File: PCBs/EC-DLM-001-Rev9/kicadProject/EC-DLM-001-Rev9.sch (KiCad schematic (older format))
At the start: 70 parts, among them J1 DMX out, J10 RJ45, J11 RJ45, J12 BARREL_JACK, J14 3.3V, J15 DMX Test pins, J2 DMX in, J20 CONN_01X04, J22 btn 6, J23 btn 3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

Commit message: Working on DLM pcb rev9
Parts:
- removed C23, C24: 100n, Capacitors_SMD:C_0603_HandSoldering, symbol C
- removed C7: 100u, Capacitors_SMD:C_0603_HandSoldering, symbol CP1
- removed J22: btn 6, Pin_Headers:Pin_Header_Straight_1x01_Pitch2.54mm, symbol CONN_01X01
- removed J23: btn 3, Pin_Headers:Pin_Header_Straight_1x01_Pitch2.54mm, symbol CONN_01X01
- removed J?: CONN_01X14, symbol CONN_01X14
- removed R15, R16: 10k, Resistors_SMD:R_0603_HandSoldering, symbol R
- removed R22, R23: 220, Resistors_SMD:R_0603_HandSoldering, symbol R
- added L1: Fer Bead, Inductors_SMD:L_0603_HandSoldering, symbol Ferrite_Bead
- added L4: 10uH, Inductors_SMD:L_0603_HandSoldering, symbol L
- F1: renamed from F?; footprint (none) -> Fuse_Holders_and_Fuses:Fuseholder5x20_horiz_open_lateral_Type-II
- J20: value CONN_01X04 -> BTN-VDD; symbol CONN_01X04 -> CONN_01X02
- gave numbers to parts that had none: 1
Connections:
- net labels added: AVCC
- net labels removed: PE3, PE4, PE5
- wire segments 304 -> 290
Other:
- moved on the sheet: C1, C17, C2, C21, C22, C3, C5, C6, C8, D3, D4, F1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

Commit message: TR04 + DLM01 REV9 adjustments.
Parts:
- removed JP1: Jumper_NC_Small, symbol Jumper_NC_Small
- added C4: 1000u, Capacitors_THT:CP_Radial_D14.0mm_P7.50mm, symbol CP1
- added J13: Bluetooth Module, Pin_Headers:Pin_Header_Straight_1x06_Pitch2.54mm, symbol CONN_01X06
- added L5: 10uH, Diodes_THT:D_DO-15_P12.70mm_Horizontal, symbol L
- L1, L4: footprint Inductors_SMD:L_0603_HandSoldering -> Diodes_THT:D_DO-15_P12.70mm_Horizontal
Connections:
- net +5V: now also J13.2 (P2)
- net AVCC: now also C4.1
- net AnalogGND: now also C4.2, L5.2
- net GND: now also J2.1, J13.3 (P3), L5.1
- net BT_TX: now reaches U3.22 (MISO/RXD1/~OC0DLS~/PC6)
- net BT_TX: now also J13.4 (P4)
- net BTN3: no longer names the net of U3.33 (PD7/TXD1/D+/SCK/CLKOUT/EVOUT)
- net BTN4: no longer names the net of U3.26 (OC0A/PD0)
- net L7_OUT_3.3: no longer names the net of U3.4 (AC1OUT/AC6/ADC6/PA6)
- net L8_OUT_3.3: no longer names the net of U3.5 (AC0OUT/AC7/ADC7/PA7)
- net STrig1: no longer names the net of U3.16 (SDAIN/SDA/~OC0ALS~/OC0A/PC0)
- net STrig2: no longer names the net of U3.17 (SCLIN/SCL/XCK0/OC0AHS/OC0B/PC1)
- net STrig3: no longer names the net of U3.18 (SDAOUT/RXD0/~OC0BLS~/OC0C/PC2)
- net STrig4: no longer names the net of U3.19 (SCLOUT/TXD0/OC0BHS/OC0D/PC3)
- net STrig5: no longer names the net of U3.20 (~SS~/~OC0CLS~/OC1A/PC4)
- net STrig6 renamed BT_RX
- net BT_RX: now also J13.5 (P5)
- no-connect marks 35 -> 45
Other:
- note added: "2 Buttons circuit"
- note added: "Bluetooth Interface (SPI)"
- note added: "DMX interface (UART)"
- note added: "External boards interfaces"
- note added: "LCD interface (SPI)"
- note added: "LED Signal 3.3v to 5V step up"
- note added: "PDI debug/prog interface"
- note added: "Power supply for microcontroller and analog"
- note added: "Rotary encoder circuit"
- note added: "User feedback LEDs"
- note added: "XMega power filtering"
- moved on the sheet: F1, L1, L4

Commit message: New Main board.
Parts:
- removed J14: 3.3V, Pin_Headers:Pin_Header_Straight_1x02_Pitch2.54mm, symbol CONN_01X02
- removed L1: Fer Bead, Diodes_THT:D_DO-15_P12.70mm_Horizontal, symbol Ferrite_Bead
- added C19: 100n, Capacitors_SMD:C_0805_HandSoldering, symbol CP1
- added C20: 68u, Capacitors_SMD:C_0805_HandSoldering, symbol CP1
- added C7: 39p, Capacitors_SMD:C_0805_HandSoldering, symbol CP1
- added D2: D_Schottky, Diodes_THT:D_A-405_P5.08mm_Vertical_AnodeUp, symbol D_Schottky
- added R11: 200k, Resistors_SMD:R_0805_HandSoldering, symbol R
- added R12: 500, Resistors_SMD:R_0805_HandSoldering, symbol R
- added R5: 17.3k, Resistors_SMD:R_0805_HandSoldering, symbol R
- added R8: 150k, Resistors_SMD:R_0805_HandSoldering, symbol R
- added U6: LM2621, Housings_SSOP:VSSOP-8_3.0x3.0mm_Pitch0.65mm, symbol LM2621
- C10, C11, C12, C13, C14, C18, C21, C22, C3, C6, C8, C9: footprint Capacitors_SMD:C_0603_HandSoldering -> Capacitors_SMD:C_0805_HandSoldering
- C17: footprint Capacitors_THT:CP_Radial_D14.0mm_P7.50mm -> Capacitors_THT:CP_Radial_D13.0mm_P5.00mm
- C4: value 1000u -> 22u; footprint Capacitors_THT:CP_Radial_D14.0mm_P7.50mm -> Capacitors_SMD:C_0805_HandSoldering
- L2, L3: footprint Inductors_SMD:L_0603_HandSoldering -> Inductors_SMD:L_0805_HandSoldering
- L4: value 10uH -> 6.8uH; footprint Diodes_THT:D_DO-15_P12.70mm_Horizontal -> Inductors_SMD:L_0805_HandSoldering
- L5: footprint Diodes_THT:D_DO-15_P12.70mm_Horizontal -> Inductors_SMD:L_0805_HandSoldering
- R1, R10, R17, R18, R24, R25, R4, R7, R9: footprint Resistors_SMD:R_0603_HandSoldering -> Resistors_SMD:R_0805_HandSoldering
- U1: footprint TO_SOT_Packages_THT:TO-220_Vertical -> TO_SOT_Packages_THT:TO-220-3_Vertical
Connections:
- net labels added: 12v
- wire segments 291 -> 387
- no-connect marks 45 -> 43
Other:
- note added: "PDI debug/prog"
- note added: "Power supply for microcontroller (up) and analog (down)"
- note removed: "PDI debug/prog interface"
- note removed: "Power supply for microcontroller and analog"
- moved on the sheet: C1, C17, C2, C5, F1, J12, J3, J5, L4, L5, R2, R3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

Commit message: Revision board rev9
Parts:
- removed C20: 68u, Capacitors_SMD:C_0805_HandSoldering, symbol CP1
- removed R12: 500, Resistors_SMD:R_0805_HandSoldering, symbol R
- removed U6: LM2621, Housings_SSOP:VSSOP-8_3.0x3.0mm_Pitch0.65mm, symbol LM2621
- added C20, C23, C24, C25, C26, C27, C28, C29, C30: 100n, symbol C
- added U6: LM2577, TO_SOT_Packages_THT:TO-220-5_Vertical, symbol LM2577
- C16, C2: value 10u -> 10u-tant
- C19: value 100n -> 680u; footprint Capacitors_SMD:C_0805_HandSoldering -> Capacitors_THT:CP_Radial_D13.0mm_P7.50mm
- C4: value 22u -> 0.33u; footprint Capacitors_SMD:C_0805_HandSoldering -> Capacitors_THT:CP_Radial_D5.0mm_P2.50mm
- C7: value 39p -> 0.1u; footprint Capacitors_SMD:C_0805_HandSoldering -> Capacitors_THT:CP_Radial_D5.0mm_P2.50mm
- D2: value D_Schottky -> 1N5821; footprint Diodes_THT:D_A-405_P5.08mm_Vertical_AnodeUp -> TO_SOT_Packages_THT:TO-220-2_Vertical
- L4: value 6.8uH -> 100uH; footprint Inductors_SMD:L_0805_HandSoldering -> Inductors_THT:L_Radial_D9.5mm_P5.00mm_Fastron_07HVP
- L5: footprint Inductors_SMD:L_0805_HandSoldering -> Inductors_THT:L_Axial_L9.5mm_D4.0mm_P5.08mm_Vertical_Fastron_SMCC
- R11: value 200k -> 2k; footprint Resistors_SMD:R_0805_HandSoldering -> Resistors_THT:R_Axial_DIN0207_L6.3mm_D2.5mm_P10.16mm_Horizontal
- R5: footprint Resistors_SMD:R_0805_HandSoldering -> Resistors_THT:R_Axial_DIN0207_L6.3mm_D2.5mm_P10.16mm_Horizontal
- R8: value 150k -> 2.2k; footprint Resistors_SMD:R_0805_HandSoldering -> Resistors_THT:R_Axial_DIN0207_L6.3mm_D2.5mm_P10.16mm_Horizontal
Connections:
- net labels added: 3.3v
- wire segments 387 -> 304
- no-connect marks 43 -> 33
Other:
- note added: "Bluetooth (SPI)"
- note removed: "Bluetooth Interface (SPI)"
- moved on the sheet: C19, C4, C7, D2, D3, L4, R11, R5, R8

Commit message: New board pour production
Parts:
- C20, C23, C24, C25, C26, C27, C28, C29, C30: footprint (none) -> Capacitors_THT:CP_Radial_D6.3mm_P2.50mm

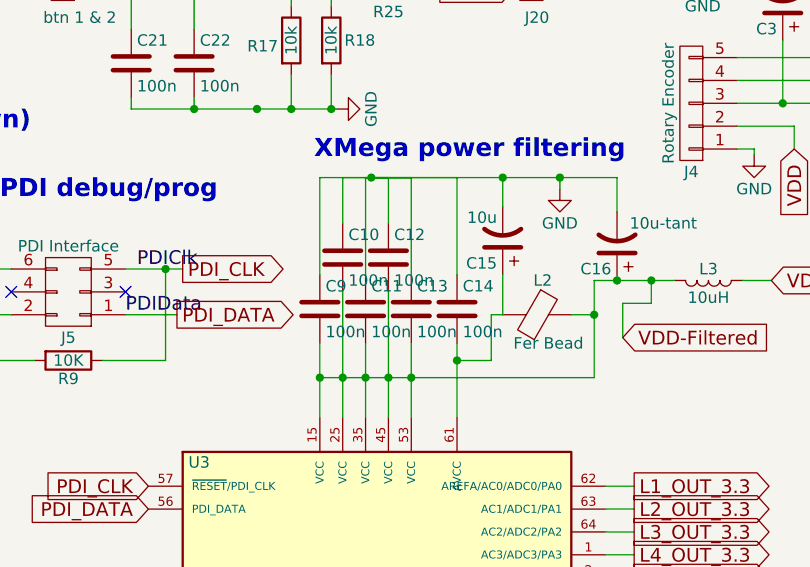
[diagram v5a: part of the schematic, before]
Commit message: Fixed screen corruption problem.
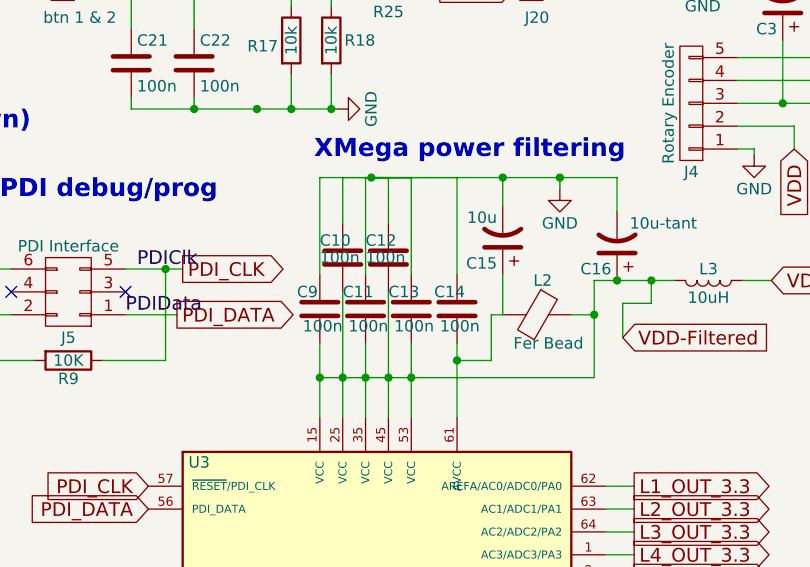
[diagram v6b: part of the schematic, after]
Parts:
- D2: footprint TO_SOT_Packages_THT:TO-220-2_Vertical -> Diodes_THT:D_DO-201AD_P15.24mm_Horizontal
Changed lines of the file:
@@
 U 1 1 59A1EB98
 P 5250 2400
-F 0 "C9" H 5275 2500 50  0000 L CNN
-F 1 "100n" H 5275 2300 50  0000 L CNN
+F 0 "C9" H 5150 2475 50  0000 L CNN
+F 1 "100n" H 5175 2325 50  0000 L CNN
 F 2 "Capacitors_SMD:C_0805_HandSoldering" H 5288 2250 50  0001 C CNN
 F 3 "" H 5250 2400 50  0001 C CNN
@@
 U 1 1 59A1EBF3
 P 5350 2175
-F 0 "C10" H 5375 2275 50  0000 L CNN
-F 1 "100n" H 5375 2075 50  0000 L CNN
+F 0 "C10" H 5250 2250 50  0000 L CNN
+F 1 "100n" H 5250 2175 50  0000 L CNN
 F 2 "Capacitors_SMD:C_0805_HandSoldering" H 5388 2025 50  0001 C CNN
 F 3 "" H 5350 2175 50  0001 C CNN
@@
 U 1 1 59A1EC2A
 P 5450 2400
-F 0 "C11" H 5475 2500 50  0000 L CNN
-F 1 "100n" H 5475 2300 50  0000 L CNN
+F 0 "C11" H 5350 2475 50  0000 L CNN
+F 1 "100n" H 5375 2325 50  0000 L CNN
 F 2 "Capacitors_SMD:C_0805_HandSoldering" H 5488 2250 50  0001 C CNN
 F 3 "" H 5450 2400 50  0001 C CNN
@@
 U 1 1 59A1EC50
 P 5550 2175
-F 0 "C12" H 5575 2275 50  0000 L CNN
-F 1 "100n" H 5575 2075 50  0000 L CNN
+F 0 "C12" H 5450 2250 50  0000 L CNN
+F 1 "100n" H 5450 2175 50  0000 L CNN
 F 2 "Capacitors_SMD:C_0805_HandSoldering" H 5588 2025 50  0001 C CNN
 F 3 "" H 5550 2175 50  0001 C CNN
@@
 U 1 1 59A1EC89
 P 5650 2400
-F 0 "C13" H 5675 2500 50  0000 L CNN
-F 1 "100n" H 5675 2300 50  0000 L CNN
+F 0 "C13" H 5550 2475 50  0000 L CNN
+F 1 "100n" H 5575 2325 50  0000 L CNN
 F 2 "Capacitors_SMD:C_0805_HandSoldering" H 5688 2250 50  0001 C CNN
 F 3 "" H 5650 2400 50  0001 C CNN
@@
 U 1 1 59A1ECBB
 P 5850 2400
-F 0 "C14" H 5875 2500 50  0000 L CNN
-F 1 "100n" H 5875 2300 50  0000 L CNN
+F 0 "C14" H 5750 2475 50  0000 L CNN
+F 1 "100n" H 5775 2325 50  0000 L CNN
 F 2 "Capacitors_SMD:C_0805_HandSoldering" H 5888 2250 50  0001 C CNN
 F 3 "" H 5850 2400 50  0001 C CNN
@@
 F 0 "D2" H 2250 2000 50  0000 C CNN
 F 1 "1N5821" H 2225 1800 50  0000 C CNN
-F 2 "TO_SOT_Packages_THT:TO-220-2_Vertical" H 2250 1900 50  0001 C CNN
+F 2 "Diodes_THT:D_DO-201AD_P15.24mm_Horizontal" H 2250 1900 50  0001 C CNN
 F 3 "" H 2250 1900 50  0001 C CNN
 	1    2250 1900
